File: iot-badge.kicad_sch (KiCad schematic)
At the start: 38 parts, among them J1 USB_C_Receptacle_USB2.0, Q1 BC847, Q2 BC847, SW1 SW_Push, SW2 SW_Push, SW3 SW_Push, SW4 SW_Push, SW5 SW_Push, SW6 SW_Push, SW7 E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

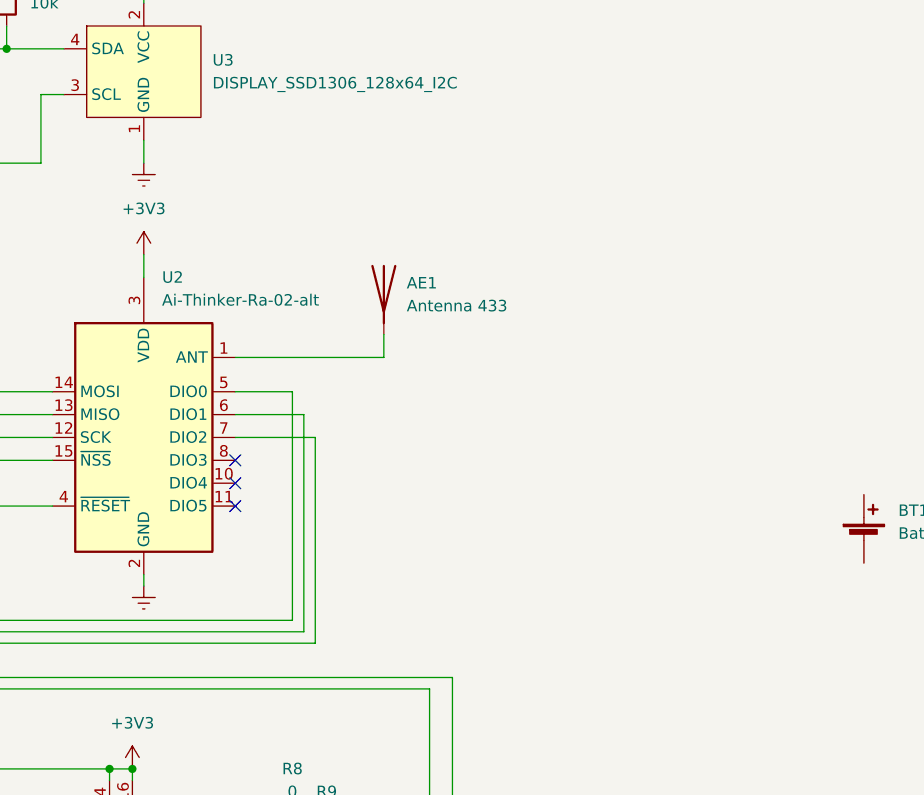
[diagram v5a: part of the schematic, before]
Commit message: added external ant
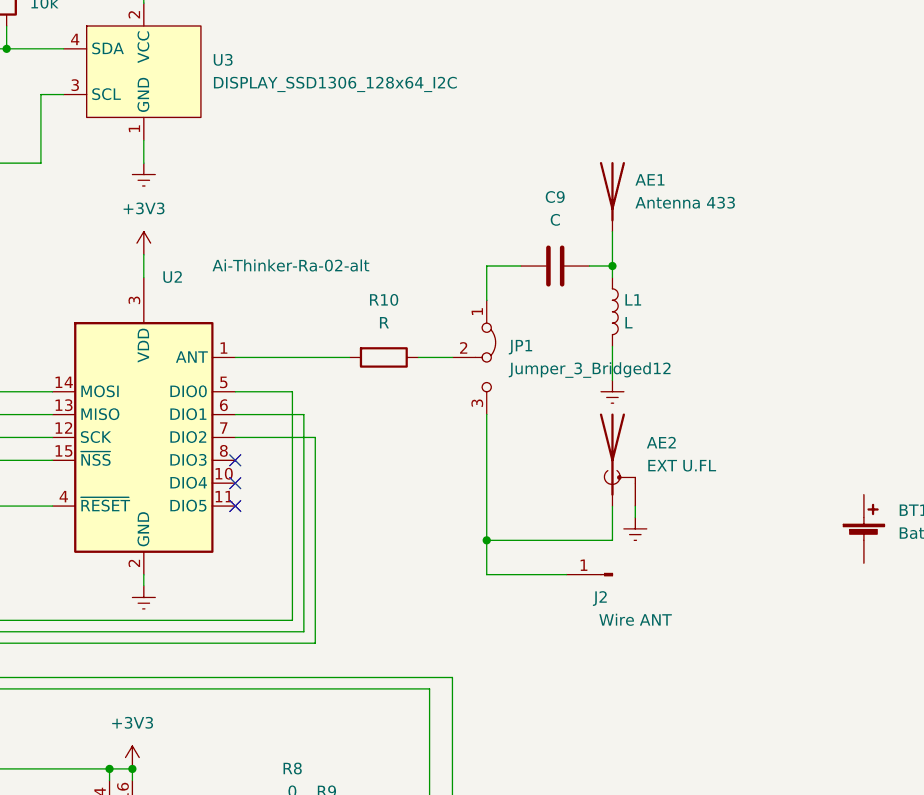
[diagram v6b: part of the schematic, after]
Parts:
- added AE2: EXT U.FL, Connector_Coaxial:U.FL_Hirose_U.FL-R-SMT-1_Vertical, symbol Device:Antenna_Shield
- added C9: C, Capacitor_SMD:C_0805_2012Metric_Pad1.18x1.45mm_HandSolder, symbol Device:C
- added J2: Wire ANT, Connector_PinHeader_1.00mm:PinHeader_1x01_P1.00mm_Vertical, symbol Connector:Conn_01x01_Male
- added JP1: Jumper_3_Bridged12, Jumper:SolderJumper-3_P1.3mm_Bridged12_RoundedPad1.0x1.5mm_NumberLabels, symbol Jumper:Jumper_3_Bridged12
- added L1: L, Inductor_SMD:L_0805_2012Metric_Pad1.05x1.20mm_HandSolder, symbol Device:L
- added R10: R, Resistor_SMD:R_0805_2012Metric_Pad1.20x1.40mm_HandSolder, symbol Device:R
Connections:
- net Earth: now also AE2.2 (Shield), L1.2
- net at U2.1 (ANT): now also R10.2; no longer AE1.1 (A)
- new net: JP1.2 (C), R10.1
- new net: AE1.1 (A), C9.1, L1.1
- new net: C9.2, JP1.1 (A)
- new net: AE2.1 (A), J2.1 (Pin_1), JP1.3 (B)
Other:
- moved on the sheet: AE1

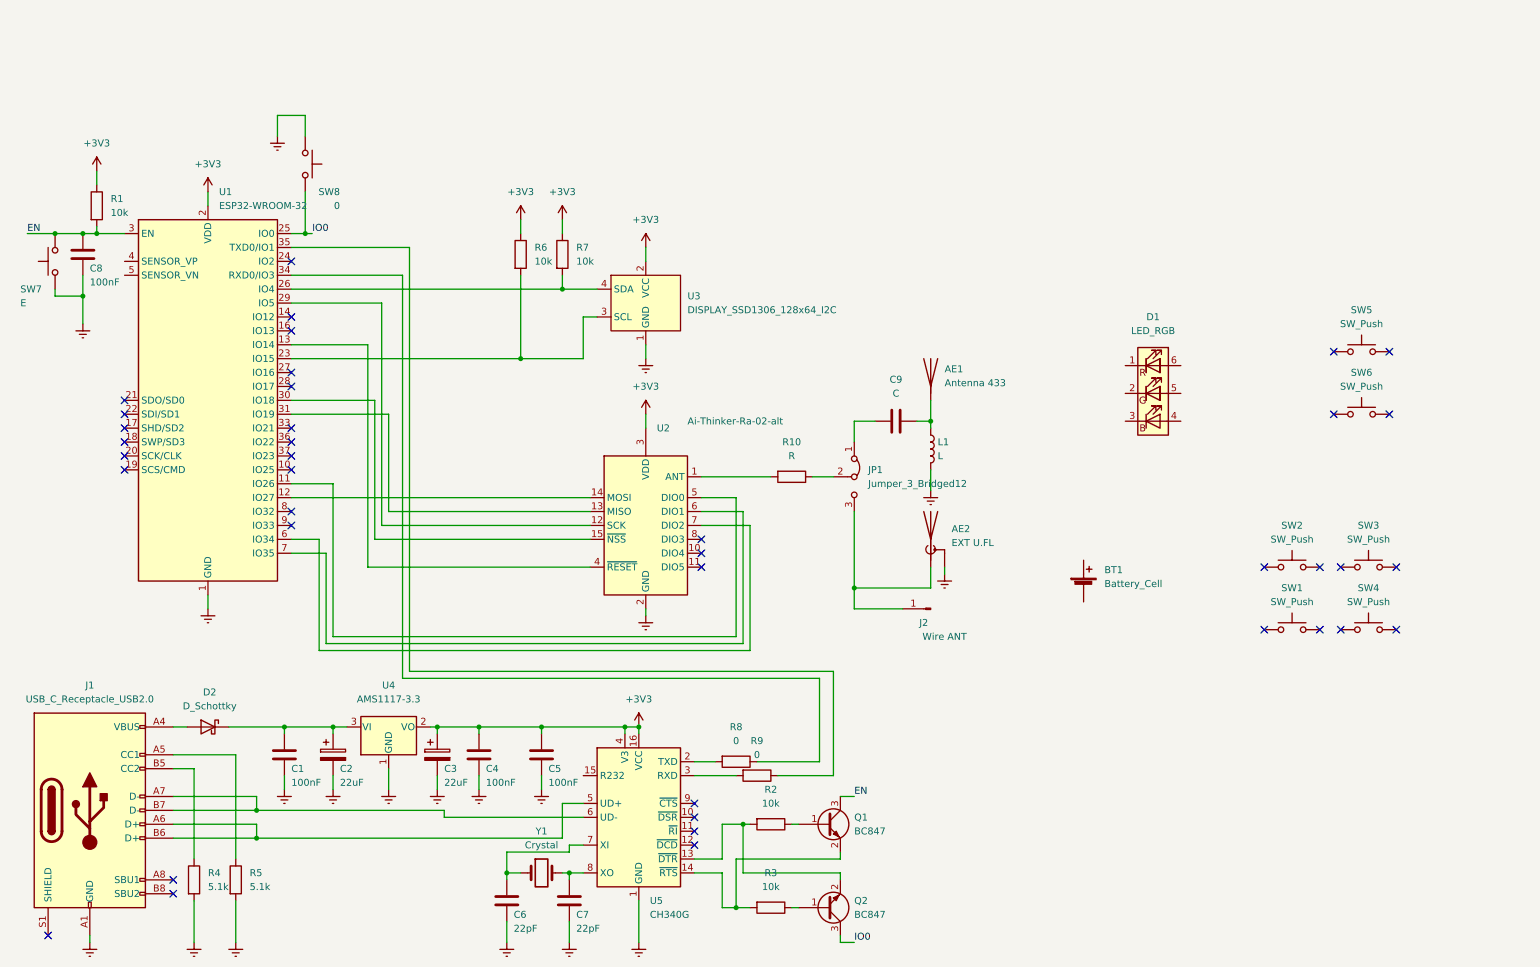
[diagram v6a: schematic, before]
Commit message: power switch added
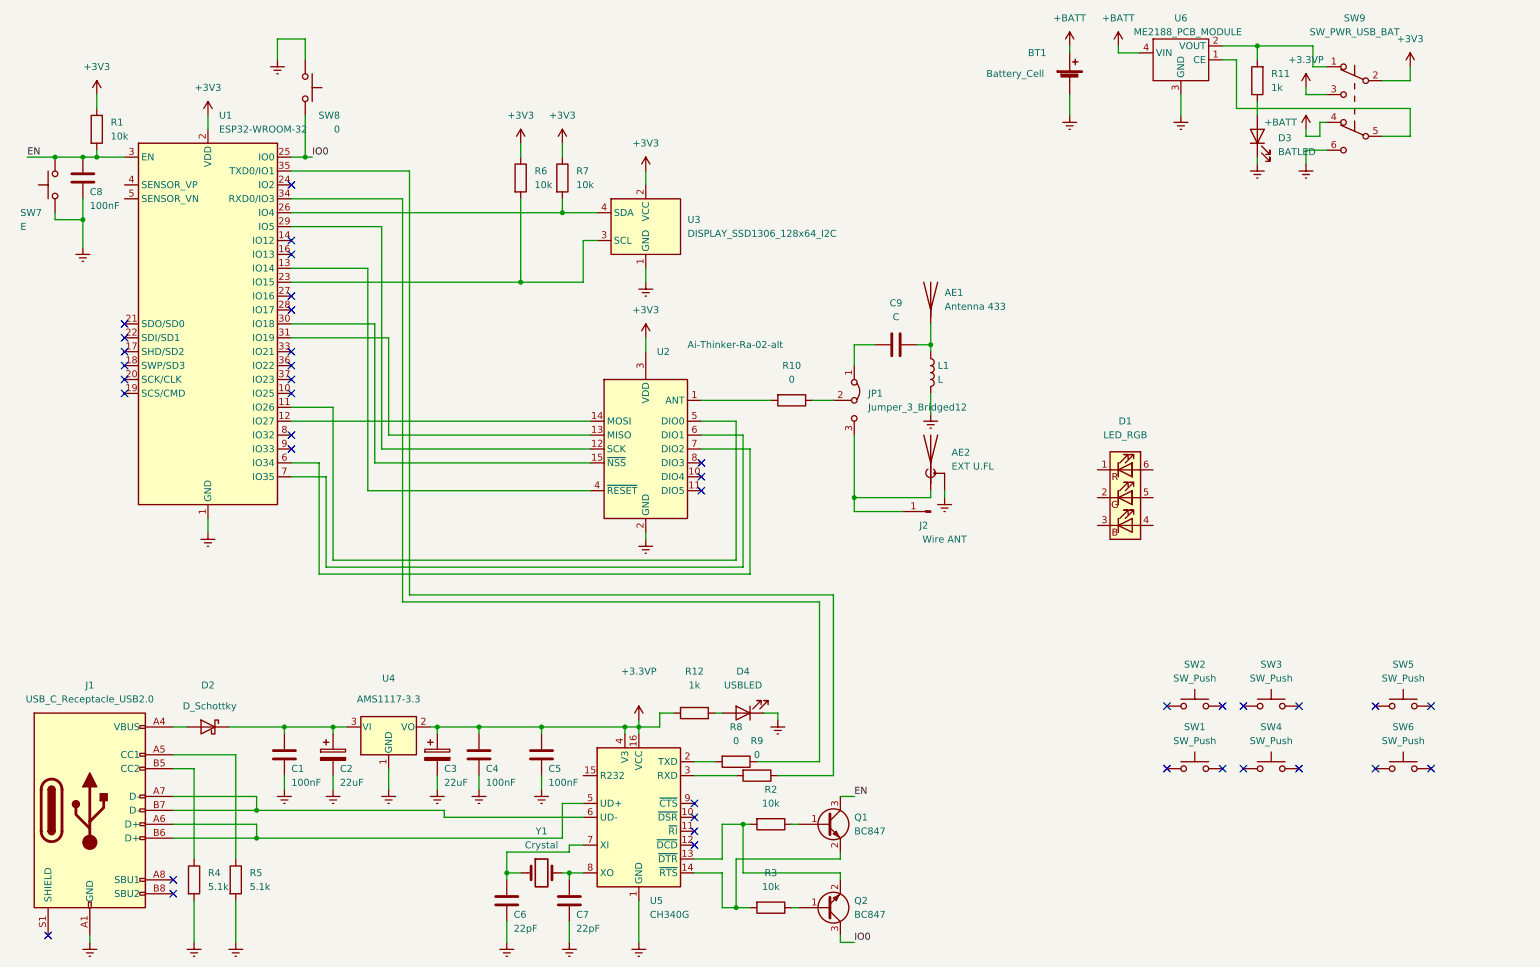
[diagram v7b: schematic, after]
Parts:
- added D3: BATLED, LED_SMD:LED_0805_2012Metric_Pad1.15x1.40mm_HandSolder, symbol Device:LED
- added D4: USBLED, LED_SMD:LED_0805_2012Metric_Pad1.15x1.40mm_HandSolder, symbol Device:LED
- added R11, R12: 1k, Resistor_SMD:R_0805_2012Metric_Pad1.20x1.40mm_HandSolder, symbol Device:R
- added SW9: SW_PWR_USB_BAT, Slide_Switch_SMD:SW_Slide_2P2T_9mmx7.6mm, symbol Switch:SW_Push_DPDT
- added U6: ME2188_PCB_MODULE, DCDC_mini_PCB_module:ME2188_PCB_MODULE, symbol Converter_mini_DCDC:ME2188_PCB_MODULE
- R10: value R -> 0
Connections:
- net +3V3: now also SW9.2 (B); no longer C3.1, C4.1, C5.1, U4.2 (VO), U5.16 (VCC), U5.4 (V3)
- net Earth: now also BT1.2 (-), D3.1 (K), D4.1 (K), SW9.6 (C), U6.3 (GND)
- net +BATT: now reaches BT1.1 (+)
- net +BATT: now also SW9.4 (A), U6.4 (VIN)
- new net: R11.2, SW9.1 (A), U6.2 (VOUT)
- new net: SW9.5 (B), U6.1 (CE)
- new net: D4.2 (A), R12.1
- new net: D3.2 (A), R11.1
- new net +3.3VP: C3.1, C4.1, C5.1, R12.2, SW9.3 (C), U4.2 (VO), U5.16 (VCC), U5.4 (V3)
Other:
- moved on the sheet: AE1, AE2, BT1, C8, C9, D1, J2, JP1, L1, R1, R10, R6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

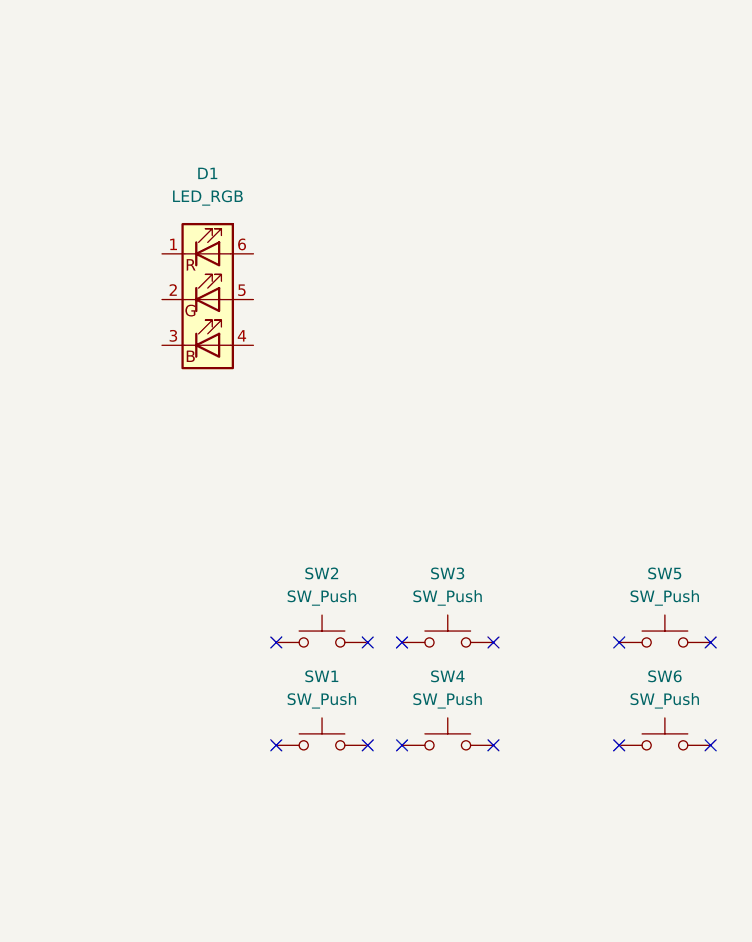
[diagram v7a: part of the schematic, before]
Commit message: added ground to pushbuttons
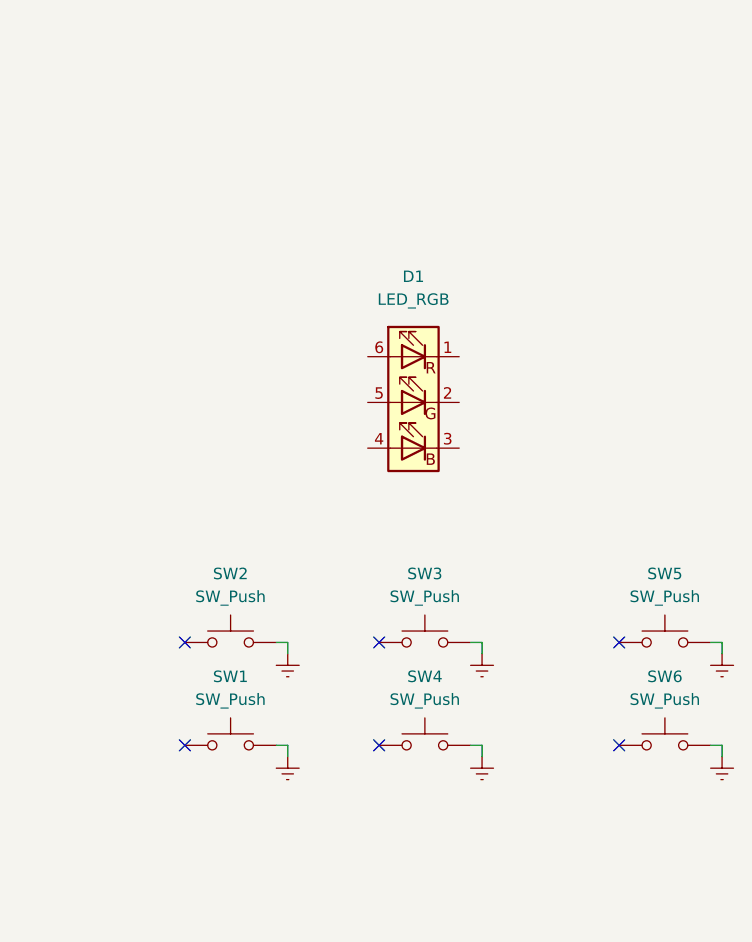
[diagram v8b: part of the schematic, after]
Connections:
- net Earth: now also SW1.2, SW2.2, SW3.2, SW4.2, SW5.2, SW6.2
- no-connect marks 39 -> 33
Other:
- moved on the sheet: D1, SW1, SW2, SW3, SW4
